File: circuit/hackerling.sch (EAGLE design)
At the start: 38 parts, among them IC1 MCP23017SP, IC2 MCP2300X/P, IC3 MIC5219BM5, SW2 SWITCH_B13EH, U1 MMA8452Q, U2 LCD-16X2NOSILK, U3 ARDUINOR3-BPLACE, U5 PCA9306, U7 POT

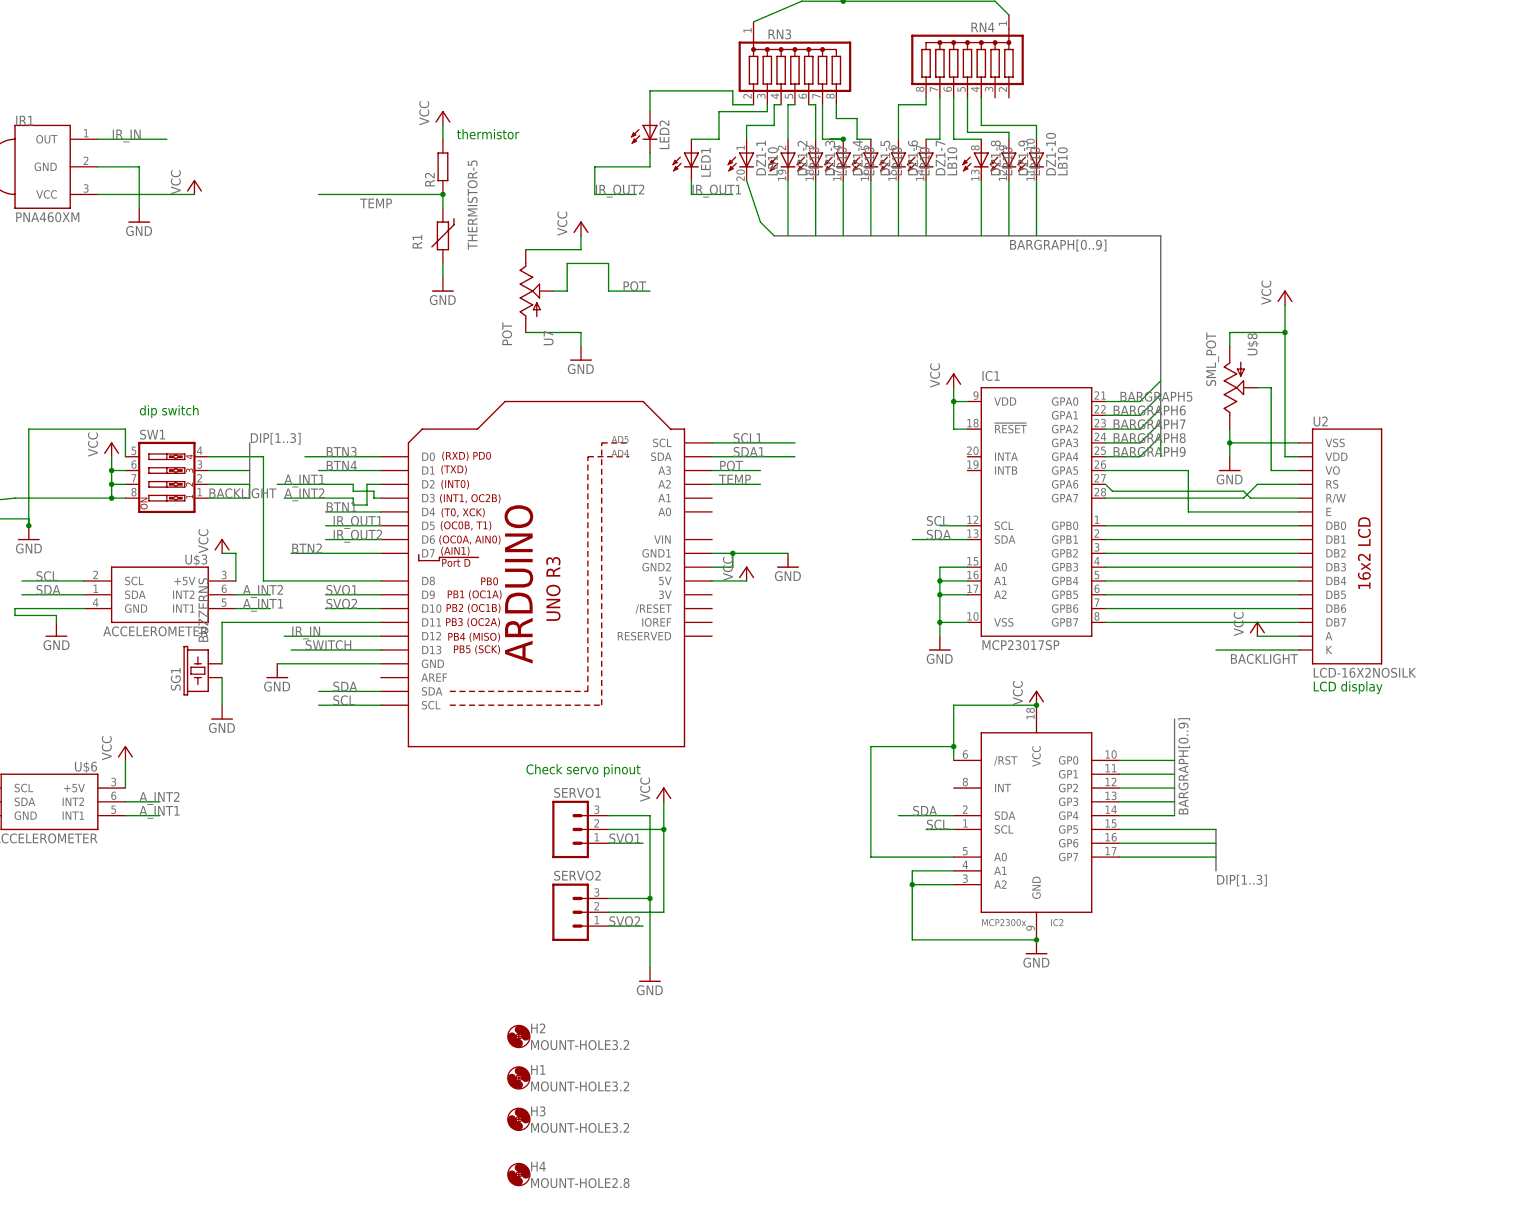
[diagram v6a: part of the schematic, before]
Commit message: adding adafruit libs to software folder
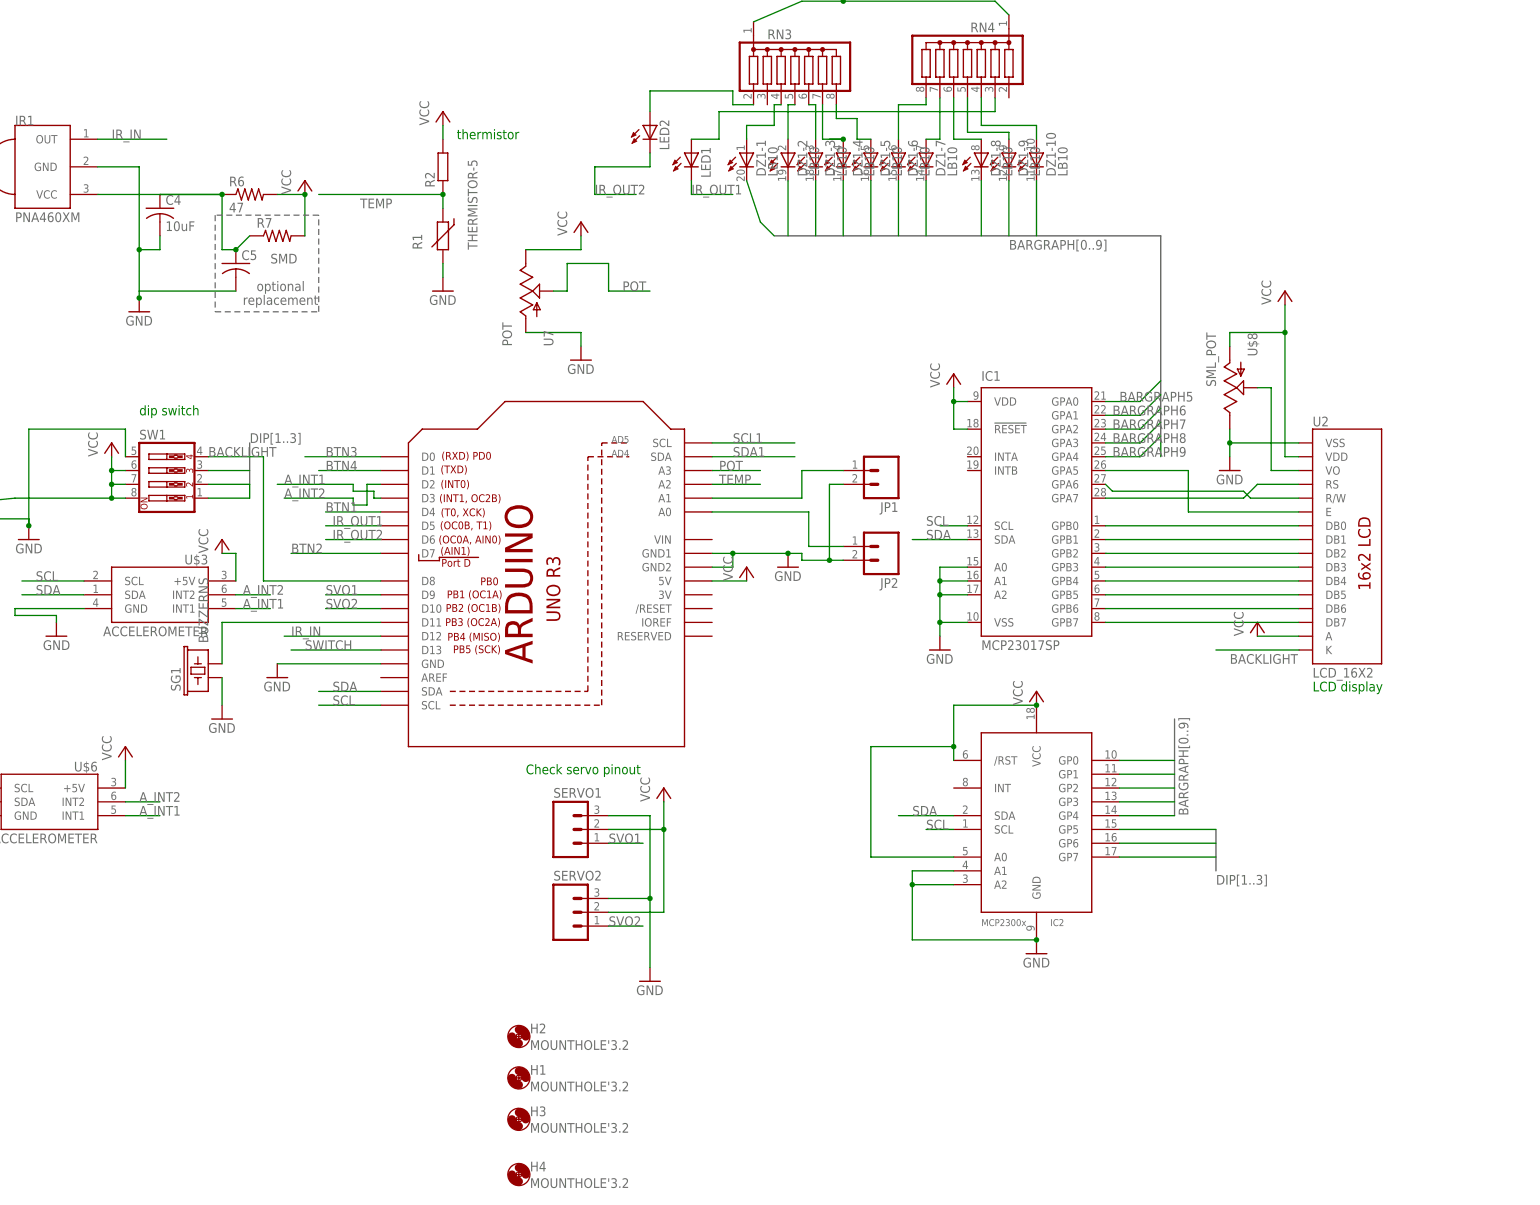
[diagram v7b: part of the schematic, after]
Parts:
- added C4: 10uF, rcl:C-US050-050X075
- added C5: (no value), resistor:C-USC0805K
- added JP1, JP2: (no value), SparkFun:M02LOCK
- added R6: 47, resistor:R-US_0204/7
- added R7: (no value), rcl:R-US_R0805
- H1, H2, H3: value MOUNT-HOLE3.2 -> MOUNTHOLE'3.2; device holes:MOUNT-HOLE3.2 -> hackerscouts:MOUNTHOLE'3.2
- H4: value MOUNT-HOLE2.8 -> MOUNTHOLE'3.2; device holes:MOUNT-HOLE2.8 -> hackerscouts:MOUNTHOLE'3.2
- U2: value LCD-16X2NOSILK -> LCD_16X2; device SparkFun:LCD-16X2NOSILK -> hackerscouts:LCD_16X2
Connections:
- new net N$19: C4.1, C5.1, IR1.VCC, R6.1, R7.1
- new net N$24: JP1.1, U3.A1
- new net N$26: JP2.1, U3.A0
- net GND: now also C4.2, C5.2, JP1.2, JP2.2
- net N$16: now also RN4.3; no longer RN3.3
- net VCC: now also R6.2, R7.2; no longer IR1.VCC
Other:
- note added: "SMD"
- note added: "optional"
- note added: "replacement"
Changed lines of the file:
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@@
 <setting verticaltext="up"/>
 </settings>
-<grid distance="0.1" unitdist="inch" unit="inch" style="lines" multiple="1" display="no" altdistance="0.01" altunitdist="inch" altunit="inch"/>
+<grid distance="0.05" unitdist="inch" unit="inch" style="lines" multiple="1" display="no" altdistance="0.01" altunitdist="inch" altunit="inch"/>
 <layers>
 <layer number="1" name="Top" color="4" fill="1" visible="no" active="no"/>
@@
 <part name="LED1" library="SparkFun" deviceset="LED" device="5MM"/>
 <part name="LED2" library="SparkFun" deviceset="LED" device="5MM"/>
-<part name="U2" library="SparkFun" deviceset="LCD-16X2" device="NOSILK"/>
+<part name="U2" library="hackerscouts" deviceset="LCD_16X2" device=""/>
 <part name="SW1" library="special" deviceset="SW_DIP-4" device=""/>
 <part name="R1" library="varistor" deviceset="THERMISTOR" device="-5"/>
@@
 <part name="P+12" library="supply1" deviceset="VCC" device=""/>
 <part name="GND11" library="supply1" deviceset="GND" device=""/>
-<part name="H2" library="holes" deviceset="MOUNT-HOLE" device="3.2"/>
-<part name="H1" library="holes" deviceset="MOUNT-HOLE" device="3.2"/>
-<part name="H3" library="holes" deviceset="MOUNT-HOLE" device="3.2"/>
+<part name="H2" library="hackerscouts" deviceset="MOUNTHOLE" device="'3.2"/>
+<part name="H1" library="hackerscouts" deviceset="MOUNTHOLE" device="'3.2"/>
+<part name="H3" library="hackerscouts" deviceset="MOUNTHOLE" device="'3.2"/>
 <part name="R3" library="SparkFun" deviceset="RESISTOR" device="0603-RES" value="4k7"/>
 <part name="GND12" library="SparkFun" deviceset="GND" device=""/>
@@
 <part name="P+16" library="supply1" deviceset="VCC" device=""/>
 <part name="GND17" library="supply1" deviceset="GND" device=""/>
-<part name="H4" library="holes" deviceset="MOUNT-HOLE" device="2.8"/>
+<part name="H4" library="hackerscouts" deviceset="MOUNTHOLE" device="'3.2"/>
 <part name="B1" library="hackerscouts" deviceset="SWITCH_BCF-4000" device=""/>
 <part name="B2" library="hackerscouts" deviceset="SWITCH_BCF-4000" device=""/>
@@
 <part name="U$8" library="hackerscouts" deviceset="SML_POT" device=""/>
 <part name="P+17" library="supply1" deviceset="VCC" device=""/>
+<part name="C4" library="rcl" deviceset="C-US" device="050-050X075" value="10uF"/>
+<part name="R6" library="resistor" deviceset="R-US_" device="0204/7" value="47"/>
+<part name="R7" library="rcl" deviceset="R-US_" device="R0805"/>
+<part name="C5" library="resistor" deviceset="C-US" device="C0805K"/>
+<part name="JP1" library="SparkFun" deviceset="M02" device="LOCK"/>
+<part name="JP2" library="SparkFun" deviceset="M02" device="LOCK"/>
 </parts>
 <sheets>
@@
 <text x="384.81" y="114.3" size="1.778" layer="91">accelerometer</text>
 <text x="50.8" y="-2.54" size="1.778" layer="91">Check servo pinout</text>
+<wire x1="12.7" y1="100.33" x2="-6.35" y2="100.33" width="0.1524" layer="95" style="shortdash"/>
+<wire x1="-6.35" y1="100.33" x2="-6.35" y2="82.55" width="0.1524" layer="95" style="shortdash"/>
+<wire x1="-6.35" y1="82.55" x2="12.7" y2="82.55" width="0.1524" layer="95" style="shortdash"/>
+<wire x1="12.7" y1="82.55" x2="12.7" y2="100.33" width="0.1524" layer="95" style="shortdash"/>
+<text x="3.81" y="91.44" size="1.778" layer="95">SMD</text>
+<text x="1.27" y="86.36" size="1.778" layer="95">optional</text>
+<text x="-1.27" y="83.82" size="1.778" layer="95">replacement</text>
 </plain>
 <instances>
@@
 <instance part="P+7" gate="VCC" x="190.5" y="86.36"/>
 <instance part="IR1" gate="G$1" x="-38.1" y="109.22"/>
-<instance part="GND9" gate="1" x="-20.32" y="99.06"/>
-<instance part="P+8" gate="VCC" x="-10.16" y="106.68"/>
+<instance part="GND9" gate="1" x="-20.32" y="82.55"/>
+<instance part="P+8" gate="VCC" x="10.16" y="106.68"/>
 <instance part="U$3" gate="G$1" x="-20.32" y="25.4" rot="MR0"/>
 <instance part="GND10" gate="1" x="-35.56" y="22.86" rot="MR0"/>
@@
 <instance part="U$8" gate="G$1" x="180.34" y="68.58" rot="MR180"/>
 <instance part="P+17" gate="VCC" x="185.42" y="25.4"/>
+<instance part="C4" gate="G$1" x="-16.51" y="101.6"/>
+<instance part="R6" gate="G$1" x="0" y="104.14"/>
+<instance part="R7" gate="G$1" x="5.08" y="96.52"/>
+<instance part="C5" gate="G$1" x="-2.54" y="91.44"/>
+<instance part="JP1" gate="G$1" x="116.84" y="53.34" rot="R180"/>
+<instance part="JP2" gate="G$1" x="116.84" y="39.37" rot="R180"/>
 </instances>
 <busses>
@@
 <wire x1="85.09" y1="38.1" x2="88.9" y2="38.1" width="0.1524" layer="91"/>
 <junction x="88.9" y="38.1"/>
+<pinref part="JP2" gate="G$1" pin="2"/>
+<wire x1="109.22" y1="36.83" x2="106.68" y2="36.83" width="0.1524" layer="91"/>
+<wire x1="106.68" y1="36.83" x2="101.6" y2="36.83" width="0.1524" layer="91"/>
+<wire x1="101.6" y1="36.83" x2="101.6" y2="38.1" width="0.1524" layer="91"/>
+<wire x1="101.6" y1="38.1" x2="99.06" y2="38.1" width="0.1524" layer="91"/>
+<junction x="99.06" y="38.1"/>
+<pinref part="JP1" gate="G$1" pin="2"/>
+<wire x1="109.22" y1="50.8" x2="106.68" y2="50.8" width="0.1524" layer="91"/>
+<wire x1="106.68" y1="50.8" x2="106.68" y2="36.83" width="0.1524" layer="91"/>
+<junction x="106.68" y="36.83"/>
 </segment>
 <segment>
@@
 <segment>
 <pinref part="GND9" gate="1" pin="GND"/>
-<wire x1="-20.32" y1="101.6" x2="-20.32" y2="109.22" width="0.1524" layer="91"/>
 <pinref part="IR1" gate="G$1" pin="GND"/>
+<wire x1="-20.32" y1="86.36" x2="-20.32" y2="93.98" width="0.1524" layer="91"/>
+<wire x1="-20.32" y1="93.98" x2="-20.32" y2="109.22" width="0.1524" layer="91"/>
 <wire x1="-20.32" y1="109.22" x2="-27.94" y2="109.22" width="0.1524" layer="91"/>
+<pinref part="C4" gate="G$1" pin="2"/>
+<wire x1="-16.51" y1="96.52" x2="-16.51" y2="93.98" width="0.1524" layer="91"/>
+<wire x1="-16.51" y1="93.98" x2="-20.32" y2="93.98" width="0.1524" layer="91"/>
+<junction x="-20.32" y="93.98"/>
+<wire x1="-20.32" y1="85.09" x2="-20.32" y2="86.36" width="0.1524" layer="91"/>
+<wire x1="-20.32" y1="86.36" x2="-2.54" y2="86.36" width="0.1524" layer="91"/>
+<junction x="-20.32" y="85.09"/>
+<pinref part="C5" gate="G$1" pin="2"/>
 </segment>
 <segment>
@@
 </segment>
 <segment>
-<pinref part="IR1" gate="G$1" pin="VCC"/>
-<pinref part="P+8" gate="VCC" pin="VCC"/>
-<wire x1="-10.16" y1="104.14" x2="-27.94" y2="104.14" width="0.1524" layer="91"/>
-</segment>
-<segment>
 <pinref part="P+10" gate="VCC" pin="VCC"/>
 <wire x1="-109.22" y1="20.32" x2="-109.22" y2="22.86" width="0.1524" layer="91"/>
@@
 <wire x1="193.04" y1="22.86" x2="185.42" y2="22.86" width="0.1524" layer="91"/>
 </segment>
+<segment>
+<pinref part="P+8" gate="VCC" pin="VCC"/>
+<pinref part="R6" gate="G$1" pin="2"/>
+<wire x1="5.08" y1="104.14" x2="10.16" y2="104.14" width="0.1524" layer="91"/>
+<pinref part="R7" gate="G$1" pin="2"/>
+<wire x1="10.16" y1="96.52" x2="10.16" y2="104.14" width="0.1524" layer="91"/>
+<junction x="10.16" y="104.14"/>
+</segment>
 </net>
 <net name="SCL" class="0">
@@
 <wire x1="24.13" y1="33.02" x2="2.54" y2="33.02" width="0.1524" layer="91"/>
 <wire x1="2.54" y1="33.02" x2="2.54" y2="55.88" width="0.1524" layer="91"/>
-<label x="-7.62" y="48.26" size="1.778" layer="95"/>
+<label x="-7.62" y="55.88" size="1.778" layer="95"/>
 <pinref part="SW1" gate="A" pin="4"/>
 <wire x1="2.54" y1="55.88" x2="-7.62" y2="55.88" width="0.1524" layer="91"/>
@@
 <pinref part="LED1" gate="G$1" pin="A"/>
 <wire x1="81.28" y1="114.3" x2="86.36" y2="114.3" width="0.1524" layer="91"/>
-<pinref part="RN3" gate="G$1" pin="3"/>
 <wire x1="86.36" y1="119.38" x2="86.36" y2="114.3" width="0.1524" layer="91"/>
-<wire x1="95.25" y1="120.65" x2="95.25" y2="119.38" width="0.1524" layer="91"/>
-<wire x1="95.25" y1="119.38" x2="86.36" y2="119.38" width="0.1524" layer="91"/>
+<pinref part="RN4" gate="G$1" pin="3"/>
+<wire x1="86.36" y1="119.38" x2="137.16" y2="119.38" width="0.1524" layer="91"/>
+<wire x1="137.16" y1="119.38" x2="137.16" y2="121.92" width="0.1524" layer="91"/>
 </segment>
 </net>
@@
 </segment>
 </net>
+<net name="N$19" class="0">
+<segment>
+<pinref part="C5" gate="G$1" pin="1"/>
+<pinref part="R7" gate="G$1" pin="1"/>
+<wire x1="0" y1="96.52" x2="-2.54" y2="93.98" width="0.1524" layer="91"/>
+<pinref part="IR1" gate="G$1" pin="VCC"/>
+<pinref part="C4" gate="G$1" pin="1"/>
+<wire x1="-5.08" y1="104.14" x2="-27.94" y2="104.14" width="0.1524" layer="91"/>
+<pinref part="R6" gate="G$1" pin="1"/>
+<junction x="-5.08" y="104.14"/>
+<wire x1="-5.08" y1="104.14" x2="-16.51" y2="104.14" width="0.1524" layer="91"/>
+<wire x1="-2.54" y1="93.98" x2="-5.08" y2="93.98" width="0.1524" layer="91"/>
+<wire x1="-5.08" y1="93.98" x2="-5.08" y2="104.14" width="0.1524" layer="91"/>
+<junction x="-2.54" y="93.98"/>
+</segment>
+</net>
+<net name="N$24" class="0">
+<segment>
+<pinref part="U3" gate="G$1" pin="A1"/>
+<wire x1="85.09" y1="48.26" x2="101.6" y2="48.26" width="0.1524" layer="91"/>
+<wire x1="101.6" y1="48.26" x2="101.6" y2="53.34" width="0.1524" layer="91"/>
+<pinref part="JP1" gate="G$1" pin="1"/>
+<wire x1="101.6" y1="53.34" x2="109.22" y2="53.34" width="0.1524" layer="91"/>
+</segment>
+</net>
+<net name="N$26" class="0">
+<segment>
+<pinref part="JP2" gate="G$1" pin="1"/>
+<wire x1="109.22" y1="39.37" x2="102.87" y2="39.37" width="0.1524" layer="91"/>
+<wire x1="102.87" y1="39.37" x2="102.87" y2="45.72" width="0.1524" layer="91"/>
+<pinref part="U3" gate="G$1" pin="A0"/>
+<wire x1="102.87" y1="45.72" x2="85.09" y2="45.72" width="0.1524" layer="91"/>
+</segment>
+</net>

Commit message: old changes to circuit adding design docs adding libraries for new chips
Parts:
- added LED3: (no value), SparkFun:LED5MM
- R7: device rcl:R-US_R0805 -> rcl:R-US_R0603
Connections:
- new net N$32: LED3.A, RN4.2
- net BTN3: now also B3.P1; no longer B3.P
- net GND: now also B2.S1, B3.S, SW1.6, SW1.7, SW1.8
- net IR_OUT1: now also LED3.C
- net VCC: no longer B1.S, B2.S1, B3.S1, B4.S1, SW1.6, SW1.7, SW1.8
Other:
- note added: "Alternate Placing"
- moved on the sheet: B1, B2, B3, B4, LED1, LED2
